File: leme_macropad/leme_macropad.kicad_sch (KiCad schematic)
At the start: 17 parts, among them J1 Rotary Encoder, J2 OLED display, SW1 SW_Push, SW2 SW_Push, SW3 SW_Push, SW4 SW_Push, SW5 SW_Push, SW6 SW_Push, SW7 SW_Push, U1 Pico

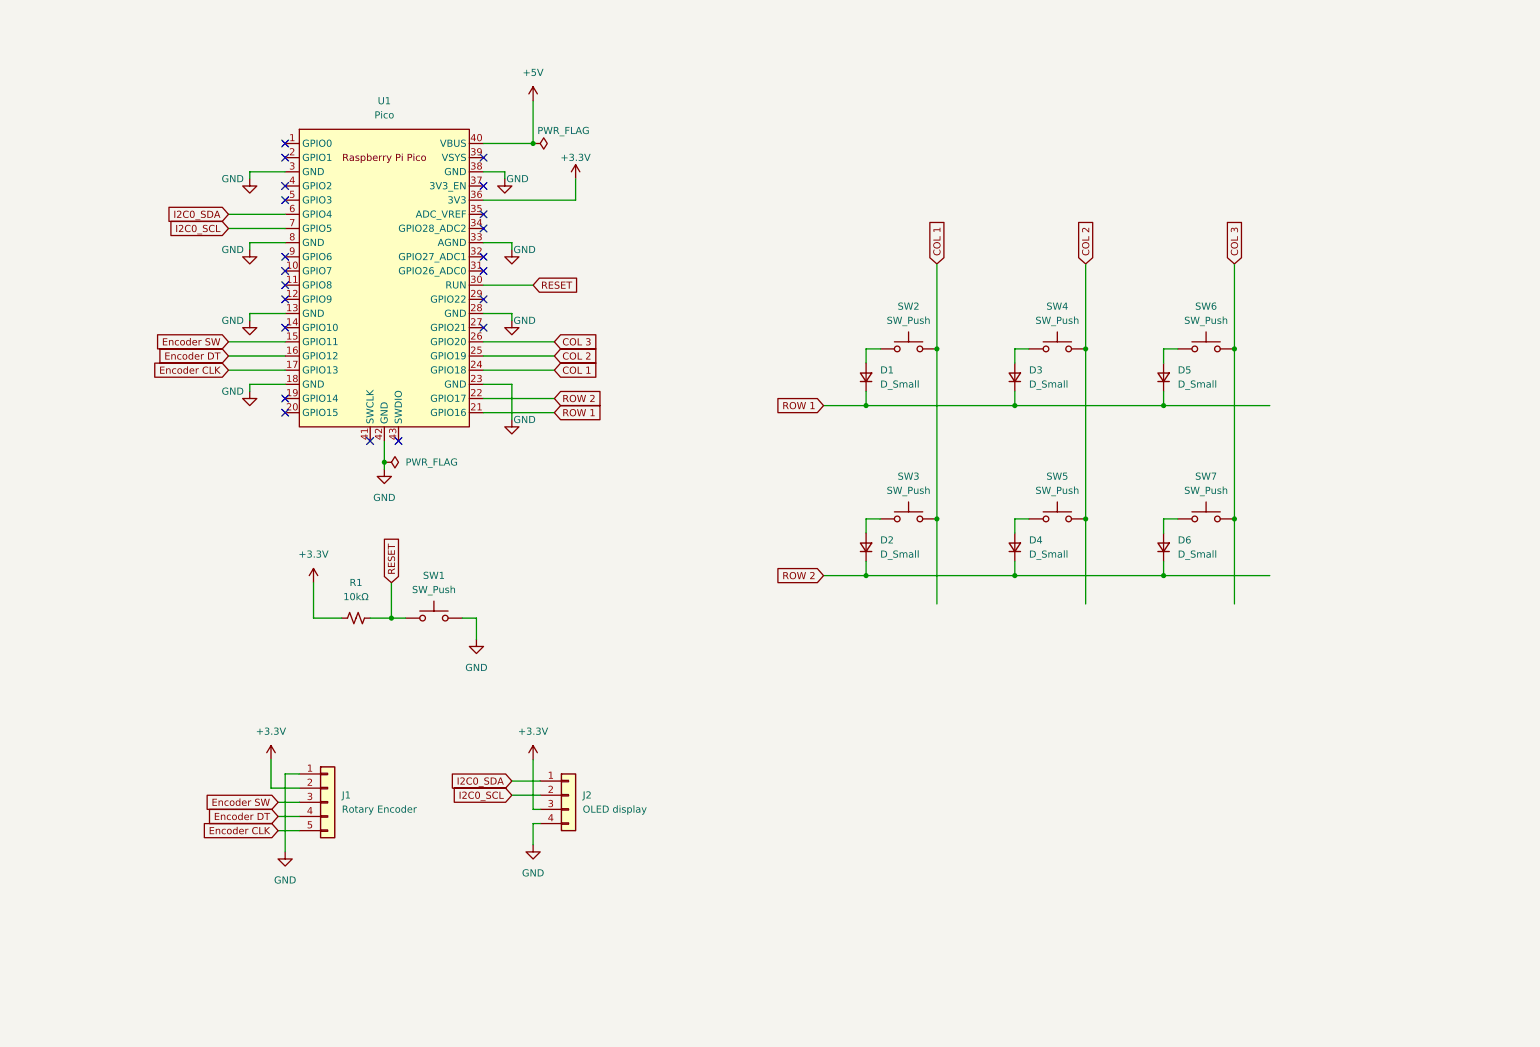
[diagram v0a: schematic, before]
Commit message: Uses rotary encoder instead of module and includes switch in matrix
The way QMK handles rotary encoder push buttons is to include it in the
switch matrix, which means I needed to add another column. Since this
opens space for an extra switch, I added it here, but it doesn't need to
be a mechanical switch as the others. We can keep the same 3x2 layout of
the main keys.

Using the encoder instead of a module is the right way to go. The
footprint for ALPS EC11E should be used when laying the PCB out because
this seems to be by far the most common format and also matches the ones
I have in stock.
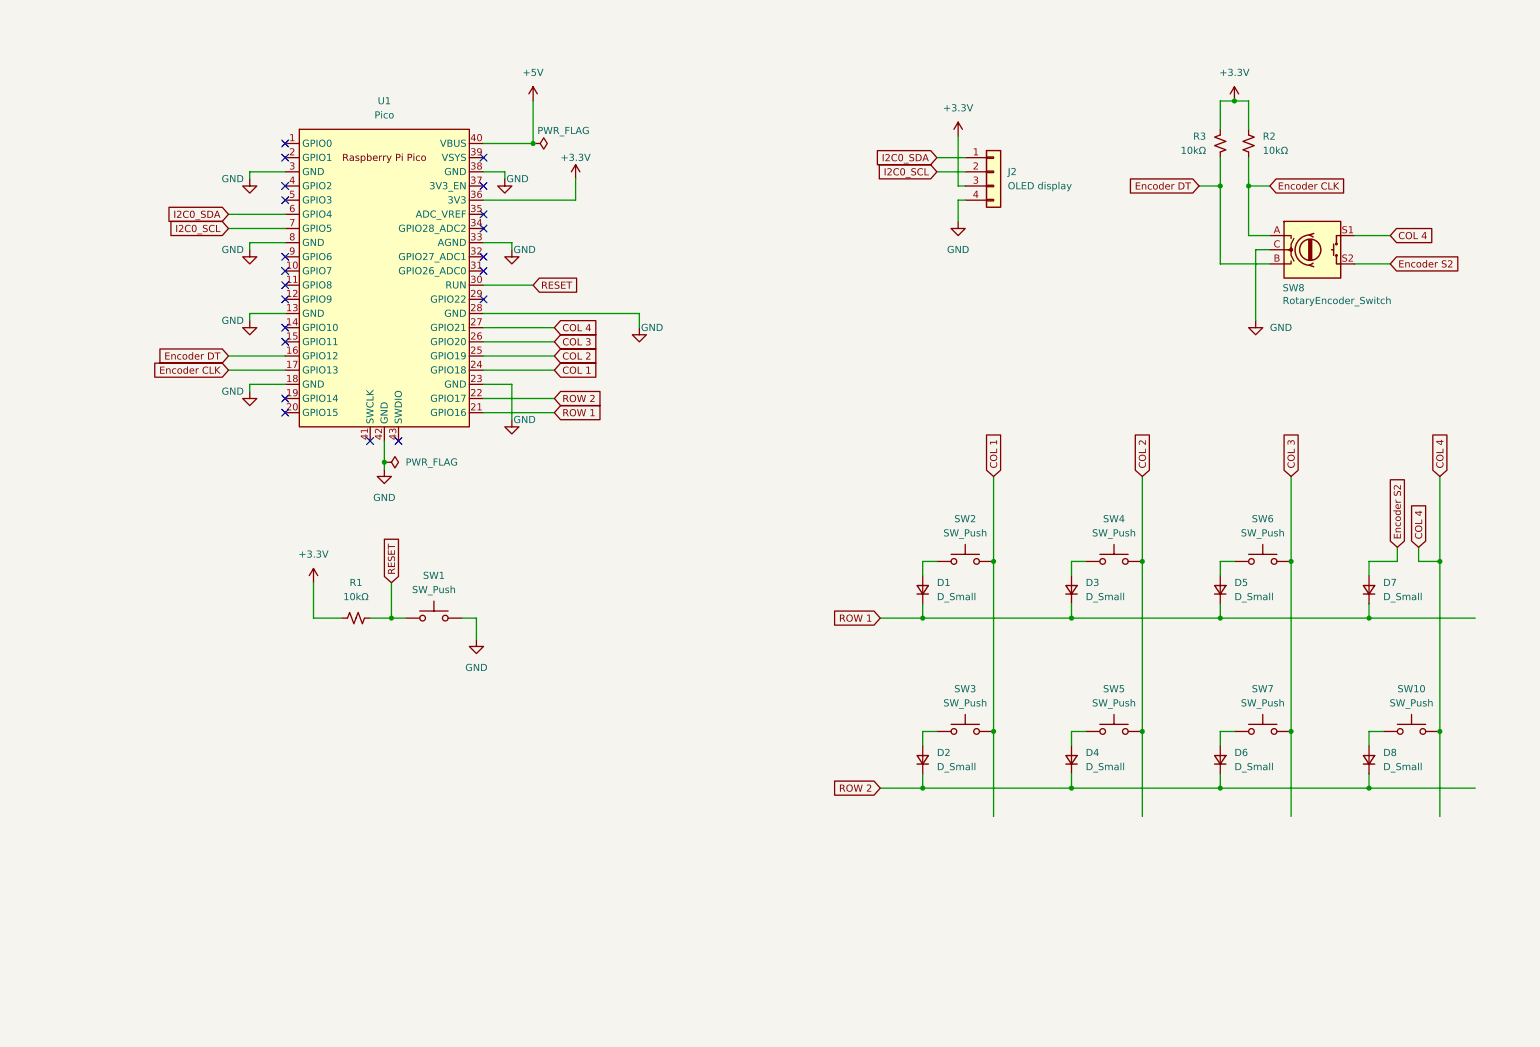
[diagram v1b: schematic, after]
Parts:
- removed J1: Rotary Encoder, symbol Connector_Generic:Conn_01x05
- added D7, D8: D_Small, symbol Device:D_Small
- added R2, R3: 10kΩ, symbol Device:R_Small_US
- added SW10: SW_Push, symbol Switch:SW_Push
- added SW8: RotaryEncoder_Switch, symbol Device:RotaryEncoder_Switch
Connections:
- net +3.3V: now also R2.2, R3.2
- net Encoder CLK: now also R2.1, SW8.A
- net Encoder DT: now also R3.1, SW8.B
- net GND: now also SW8.C
- net ROW 1: now also D7.1 (K)
- net ROW 2: now also D8.1 (K)
- net COL 4: now reaches U1.27 (GPIO21)
- net COL 4: now also SW10.2, SW8.S1
- net Encoder SW: no longer names the net of U1.15 (GPIO11)
- new net: D8.2 (A), SW10.1
- new net Encoder S2: D7.2 (A), SW8.S2
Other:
- title: (none) -> Leme macropad
- moved on the sheet: D1, D2, D3, D4, D5, D6, J2, SW2, SW3, SW4, SW5, SW6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

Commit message: Replaces Pi pico with a RP2040
This is much better for our purposes. It gives us more control, uses
much less space on the PCB and allows us to use a USB-C connector.

All the components around the RP2040 are the ones recommended in the
RP2040 hardware design guide. They not only are recommended, but also
readily available and easy enough to use.
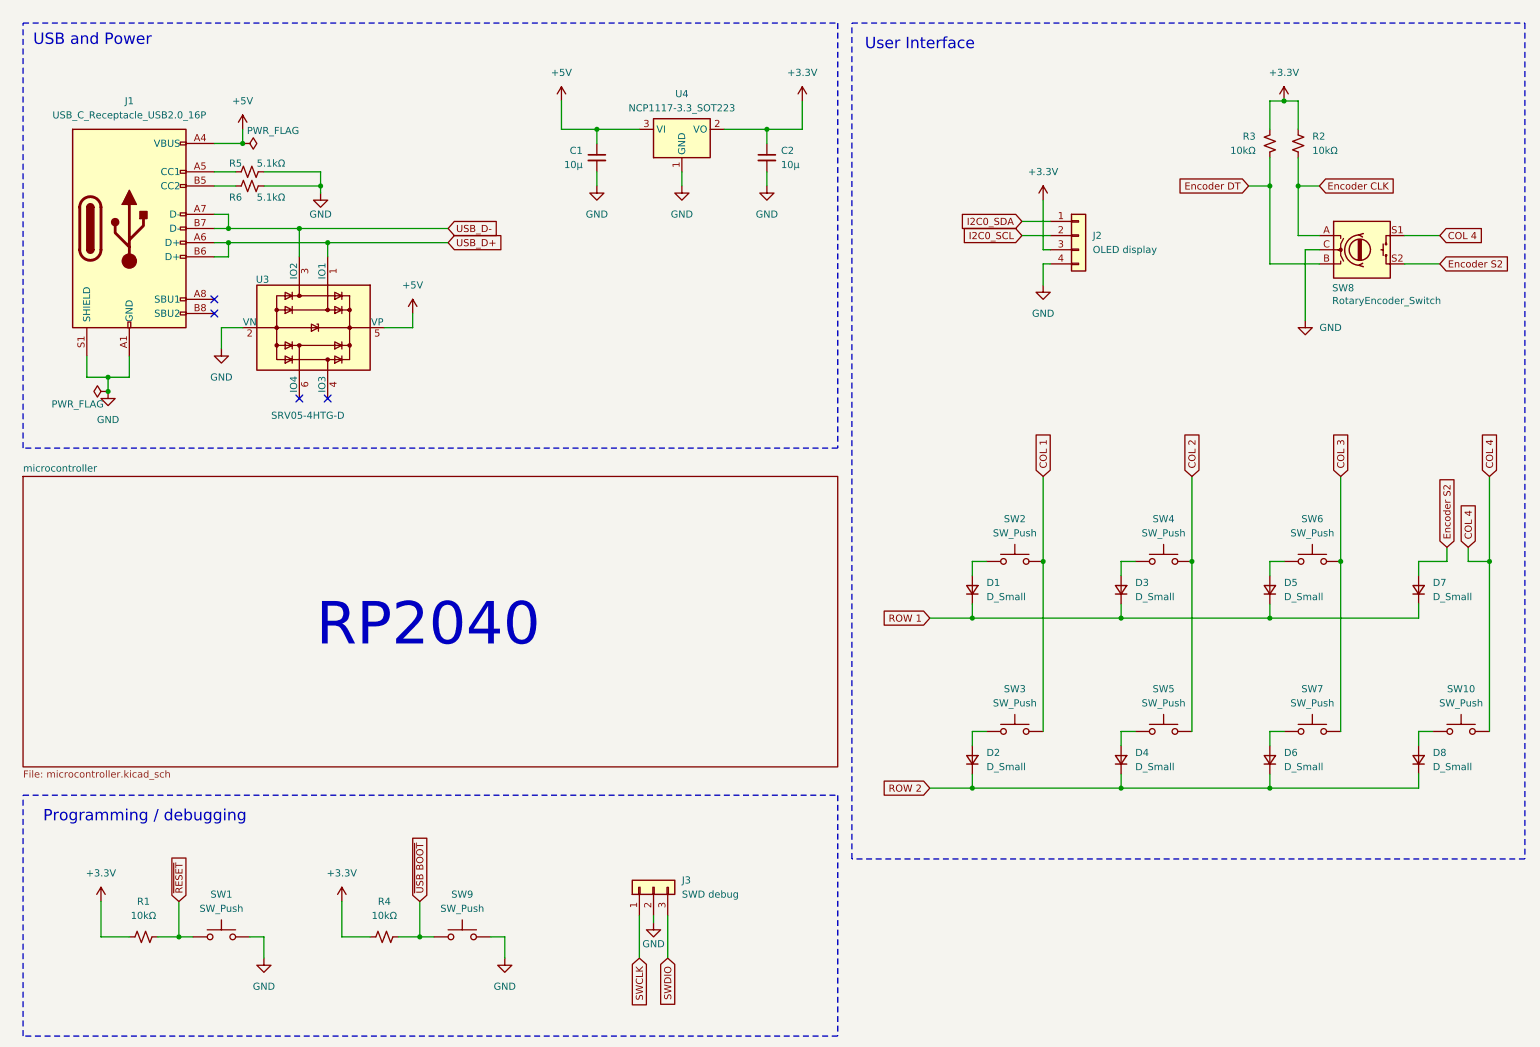
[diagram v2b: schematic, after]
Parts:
- removed U1: Pico, RPi_Pico:RPi_Pico_SMD_TH, symbol Pi_pico:Pico
- added C1, C2: 10μ, symbol Device:C_Small
- added J1: USB_C_Receptacle_USB2.0_16P, symbol Connector:USB_C_Receptacle_USB2.0_16P
- added J3: SWD debug, symbol Connector_Generic:Conn_01x03
- added R4: 10kΩ, symbol Device:R_Small_US
- added R5, R6: 5.1kΩ, symbol Device:R_Small_US
- added SW9: SW_Push, symbol Switch:SW_Push
- added U3: SRV05-4HTG-D, Package_TO_SOT_SMD:SOT-23-6, symbol Power_Protection:SRV05-4
- added U4: NCP1117-3.3_SOT223, Package_TO_SOT_SMD:SOT-223-3_TabPin2, symbol Regulator_Linear:NCP1117-3.3_SOT223
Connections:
- net +3.3V: now also C2.1, R4.1, U4.2 (VO)
- net +5V: now also C1.1, J1.A4 (VBUS), J1.A9 (VBUS), J1.B4 (VBUS), J1.B9 (VBUS), U3.5 (VP), U4.3 (VI)
- net GND: now also C1.2, C2.2, J1.A1 (GND), J1.A12 (GND), J1.B1 (GND), J1.B12 (GND), J1.S1 (SHIELD), J3.2 (Pin_2), R5.2, R6.2, SW9.2, U3.2 (VN), U4.1 (GND)
- net RESET renamed ~{RESET}
- new net: J1.A5 (CC1), R5.1
- new net: J1.B5 (CC2), R6.1
- new net SWCLK: J3.1 (Pin_1)
- new net SWDIO: J3.3 (Pin_3)
- new net USB_D+: J1.A6 (D+), J1.B6 (D+), U3.1 (IO1)
- new net USB_D-: J1.A7 (D-), J1.B7 (D-), U3.3 (IO2)
- new net ~{USB BOOT}: R4.2, SW9.1
- no-connect marks 21 -> 4
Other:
- added sheet microcontroller (microcontroller.kicad_sch)
- note added: "Programming / debugging"
- note added: "RP2040"
- note added: "USB and Power"
- note added: "User Interface"
- moved on the sheet: D1, D2, D3, D4, D5, D6, D7, D8, J2, R1, R2, R3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

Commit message: Annotates schematics again
Everything changed a lot, so it makes sense to reorder the components.
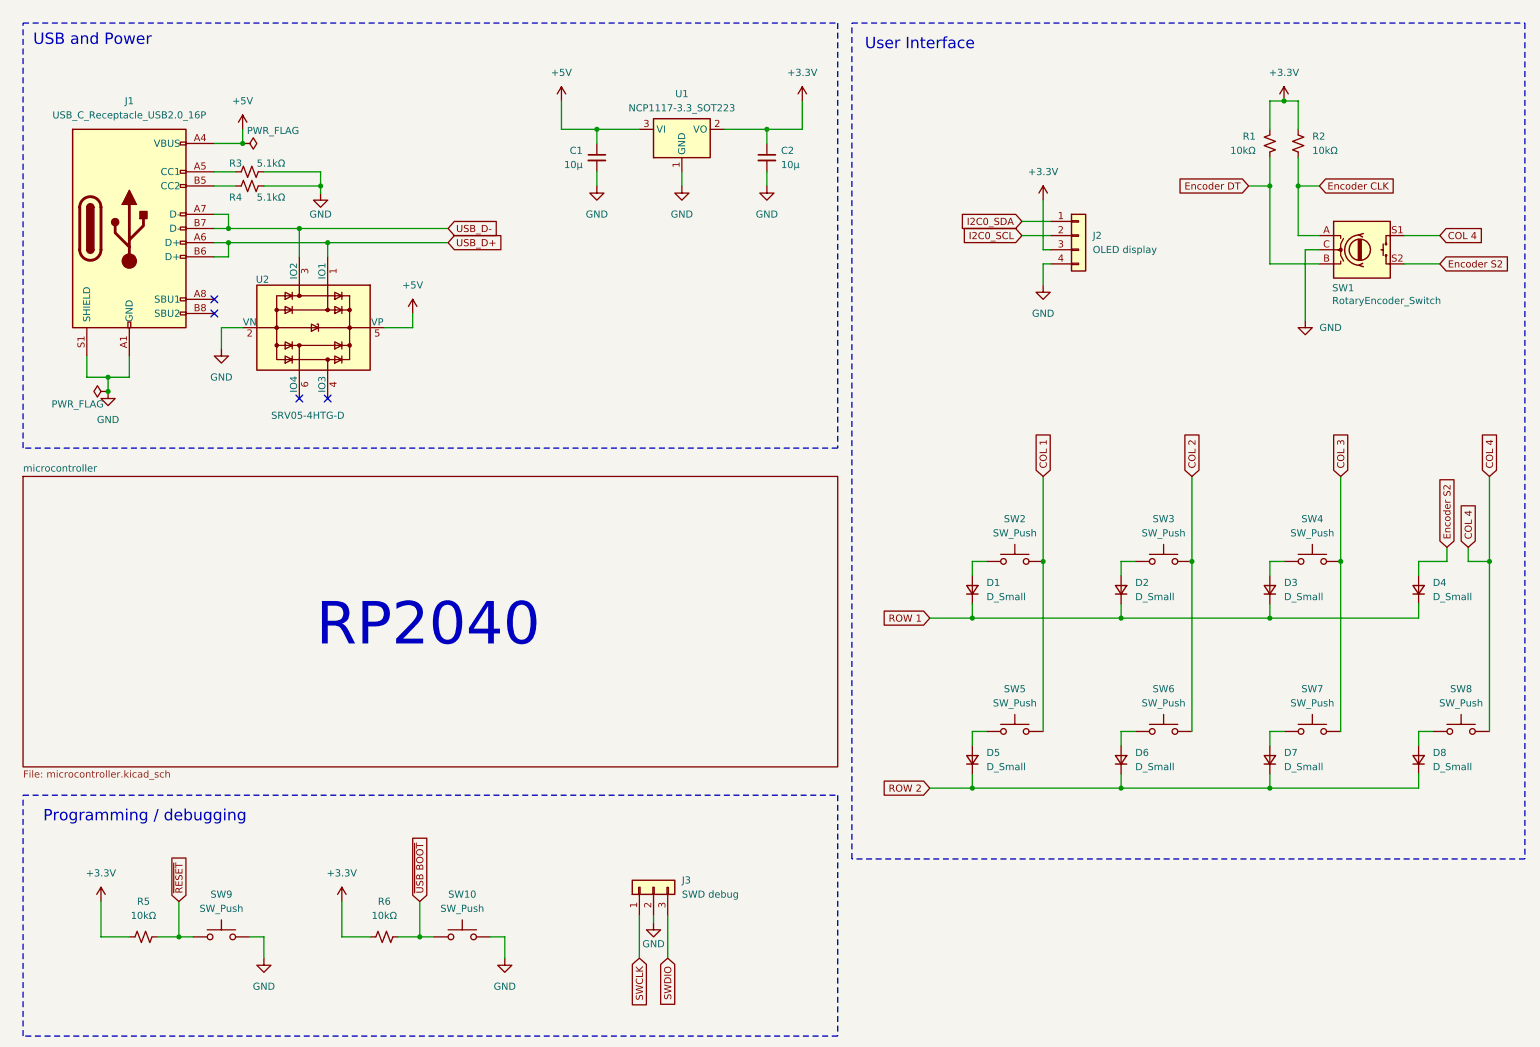
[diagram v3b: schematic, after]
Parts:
- renumbered D3 to D2, D5 to D3, D7 to D4, D2 to D5, D4 to D6, D6 to D7, R3 to R1, R5 to R3, R6 to R4, R1 to R5, R4 to R6, SW8 to SW1, SW9 to SW10, SW4 to SW3, SW6 to SW4, SW3 to SW5, SW5 to SW6, SW10 to SW8, SW1 to SW9, U4 to U1, U3 to U2

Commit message: Moves user interface to it's own hierarchical sheet
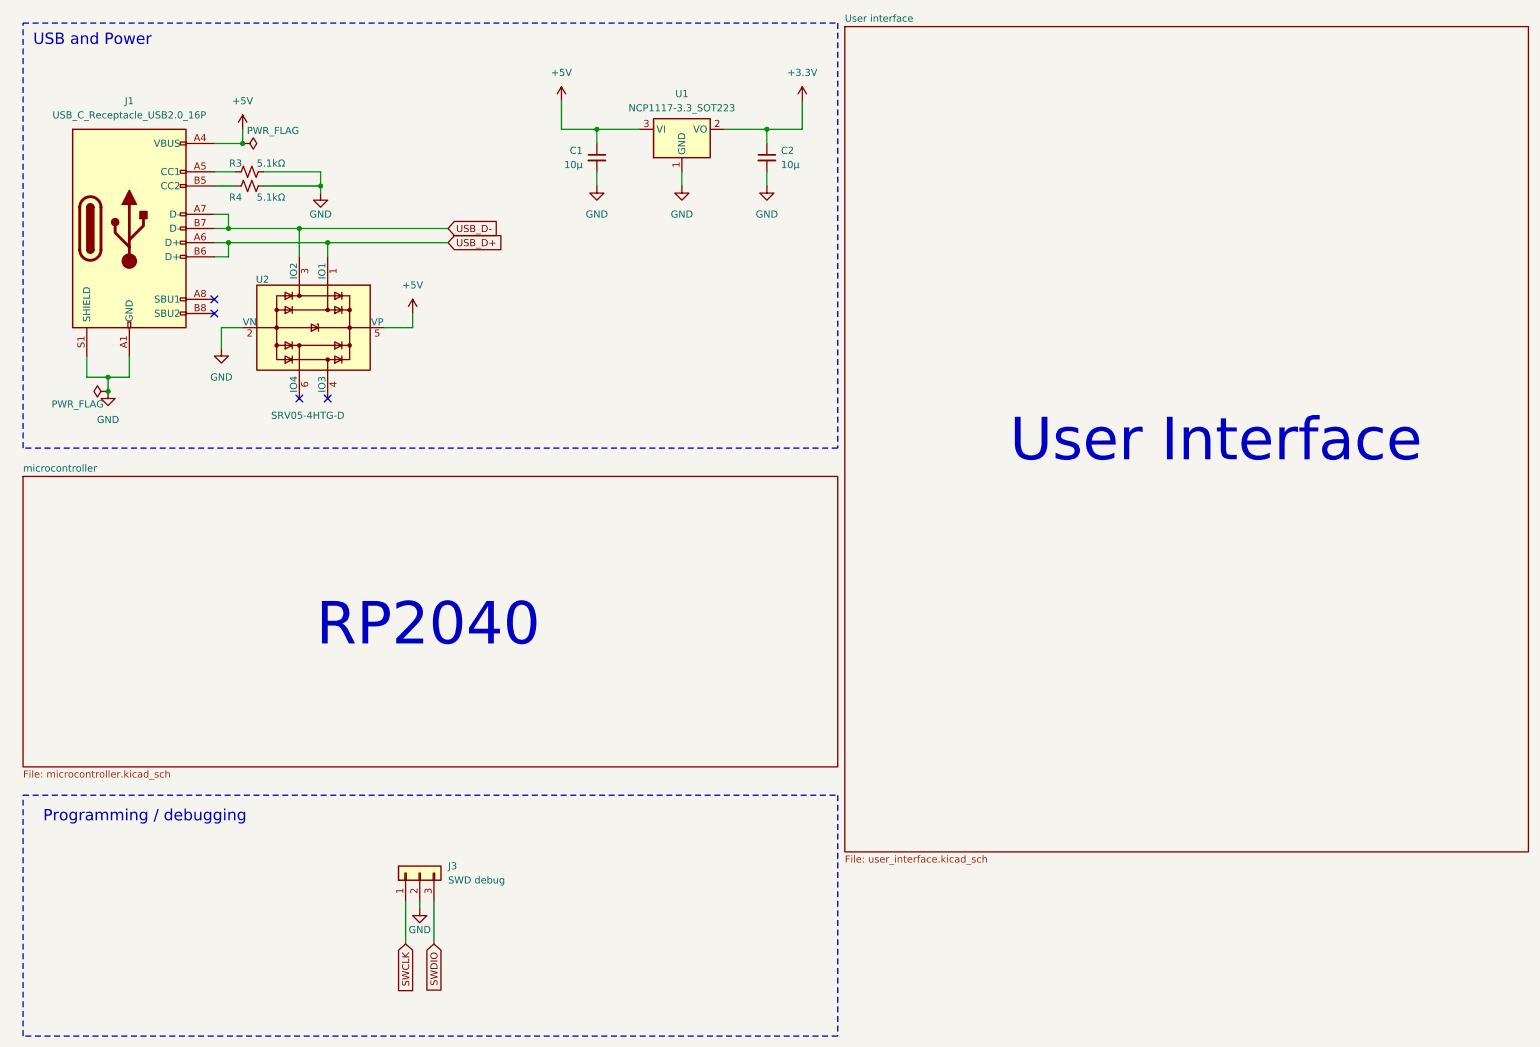
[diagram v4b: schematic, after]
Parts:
- removed D1, D2, D3, D4, D5, D6, D7, D8: D_Small, symbol Device:D_Small
- removed J2: OLED display, symbol Connector_Generic:Conn_01x04
- removed R1, R2, R5, R6: 10kΩ, symbol Device:R_Small_US
- removed SW1: RotaryEncoder_Switch, symbol Device:RotaryEncoder_Switch
- removed SW10, SW2, SW3, SW4, SW5, SW6, SW7, SW8, SW9: SW_Push, symbol Switch:SW_Push
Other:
- added sheet User interface (user_interface.kicad_sch)
- moved on the sheet: J3
